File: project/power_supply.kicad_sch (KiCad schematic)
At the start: 20 parts, among them J1 USB_C_Receptacle_USB2.0_16P, U1 LD1117S33TR_SOT223, U2 LD1117S12TR_SOT223, U3 USBLC6-2SC6

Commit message: Ruteo critico finalizado
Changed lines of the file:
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@@
 (kicad_sch
-	(version 20231120)
+	(version 20250114)
 	(generator "eeschema")
-	(generator_version "8.0")
+	(generator_version "9.0")
 	(paper "A4")
 	(junction
@@
 		(shape bidirectional)
 		(at 93.98 93.98 0)
-		(fields_autoplaced yes)
 		(effects
 			(font
@@
 		(shape output)
 		(at 149.86 96.52 270)
-		(fields_autoplaced yes)
 		(effects
 			(font
@@
 		(shape output)
 		(at 143.51 72.39 90)
-		(fields_autoplaced yes)
 		(effects
 			(font
@@
 		(shape bidirectional)
 		(at 93.98 91.44 0)
-		(fields_autoplaced yes)
 		(effects
 			(font
@@
 		(shape output)
 		(at 189.23 73.66 90)
-		(fields_autoplaced yes)
 		(effects
 			(font
@@
 		(shape output)
 		(at 252.73 76.2 0)
-		(fields_autoplaced yes)
 		(effects
 			(font

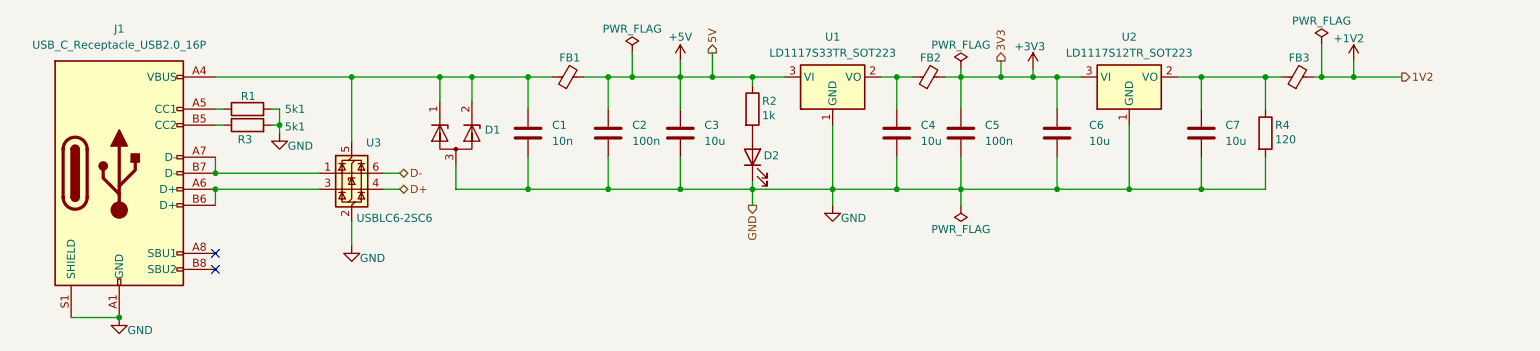
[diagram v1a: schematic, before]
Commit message: Agregado de datasheets, cambio de regulador zener, ajuste de posicion de regulador, modelo 3d de oscilador
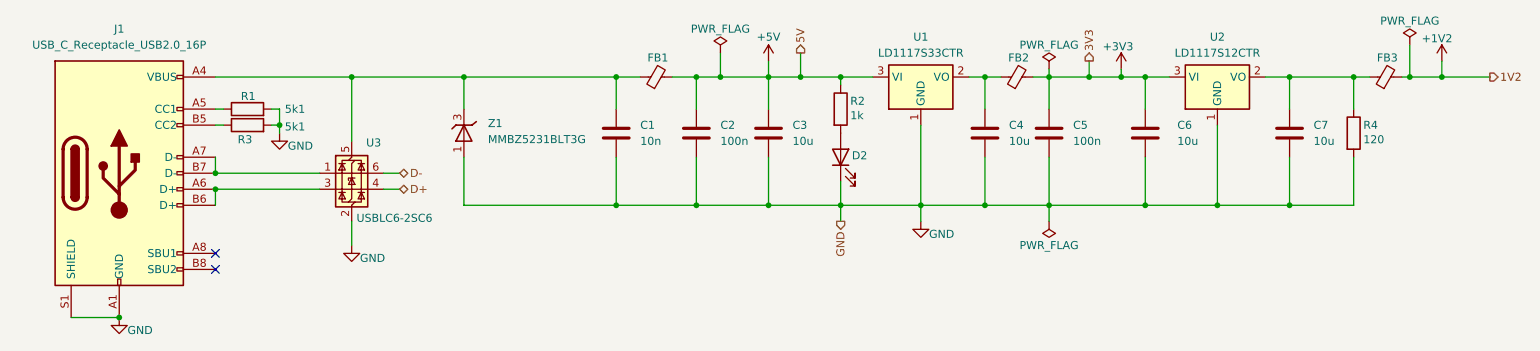
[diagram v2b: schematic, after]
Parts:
- removed D1: ~, Package_TO_SOT_SMD:SOT-23, symbol Diode:MMBZxx
- added Z1: MMBZ5231BLT3G, MMBZ5231BLT3G:SOT96P237X111-3N, symbol MMBZ5231BLT3G:MMBZ5231BLT3G
- C1: Código del fabricante (Order Code) (none) -> CL31B103KHFNFNE; Código del vendedor (Provider Order Code) (none) -> 187-CL31B103KHFNFNE; Fabricante (none) -> Samsung; Package (none) -> 1206
- C2, C5: Código del fabricante (Order Code) (none) -> CL31B104KBCNFNC; Código del vendedor (Provider Order Code) (none) -> 187-CL31B104KBCNFNC; Fabricante (none) -> Samsung; Package (none) -> 1206
- C3, C4, C6, C7: Código del fabricante (Order Code) (none) -> CL31B106KAHNNNE; Código del vendedor (Provider Order Code) (none) -> 187-CL31B106KAHNNNE; Fabricante (none) -> Samsung; Package (none) -> 1206
- D2: value LED Green -> LED Red; Código del fabricante (Order Code) (none) -> 150141RS73100; Código del vendedor (Provider Order Code) (none) -> 710-150141RS73100; Fabricante (none) -> Wurth Elektronik; Package (none) -> 3528
- FB1, FB2, FB3: Código del fabricante (Order Code) (none) -> 742792141; Código del vendedor (Provider Order Code) (none) -> 710-742792141; Fabricante (none) -> Wurth Elektronik; Package (none) -> 1206
- J1: Código del fabricante (Order Code) (none) -> GSB1C41110SSHR; Código del vendedor (Provider Order Code) (none) -> 523-GSB1C41110SSHR; Fabricante (none) -> Amphenol; Package (none) -> USB-C
- R1, R3: Código del fabricante (Order Code) (none) -> AC1206FR-075K1L; Código del vendedor (Provider Order Code) (none) -> 603-AC1206FR-075K1L; Fabricante (none) -> Yageo; Package (none) -> 1206
- R2: Código del fabricante (Order Code) (none) -> RC1206FR-101KL; Código del vendedor (Provider Order Code) (none) -> 603-RC1206FR-101KL; Fabricante (none) -> Yageo; Package (none) -> 1206
- R4: Código del fabricante (Order Code) (none) -> RC1206FR-07120RL; Código del vendedor (Provider Order Code) (none) -> 603-RC1206FR-07120RL; Fabricante (none) -> Yageo; Package (none) -> 1206
- U1: value LD1117S33TR_SOT223 -> LD1117S33CTR; Código del fabricante (Order Code) (none) -> LD1117S33CTR; Código del vendedor (Provider Order Code) (none) -> 511-LD1117S33CTR; Fabricante (none) -> ST; Package (none) -> SOT-223-3
- U2: value LD1117S12TR_SOT223 -> LD1117S12CTR; Código del fabricante (Order Code) (none) -> LD1117S12CTR; Código del vendedor (Provider Order Code) (none) -> 511-LD1117S12CTR; Fabricante (none) -> ST; Package (none) -> SOT-223-3
- U3: Código del fabricante (Order Code) (none) -> USBLC6-2SC6; Código del vendedor (Provider Order Code) (none) -> 511-USBLC6-2SC6; Fabricante (none) -> ST; Package (none) -> SOT-666-6
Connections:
- net GND: now also Z1.1
- net at C1.1, FB1.1, J1.A4 (VBUS)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: now also Z1.3
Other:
- moved on the sheet: C1, C2, C3, C4, C5, C6, C7, D2, FB1, FB2, FB3, R2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

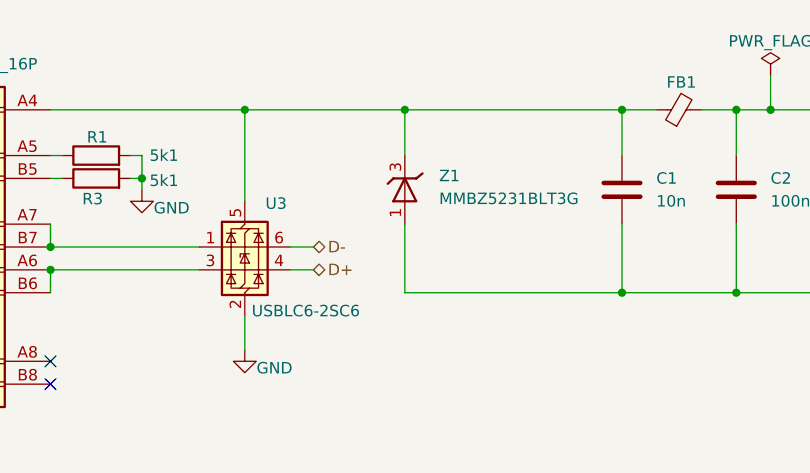
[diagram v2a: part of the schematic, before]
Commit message: Pistas, pads, soldermask y silkscreen corregidas para pasar analisis DMF de jlcpcb.
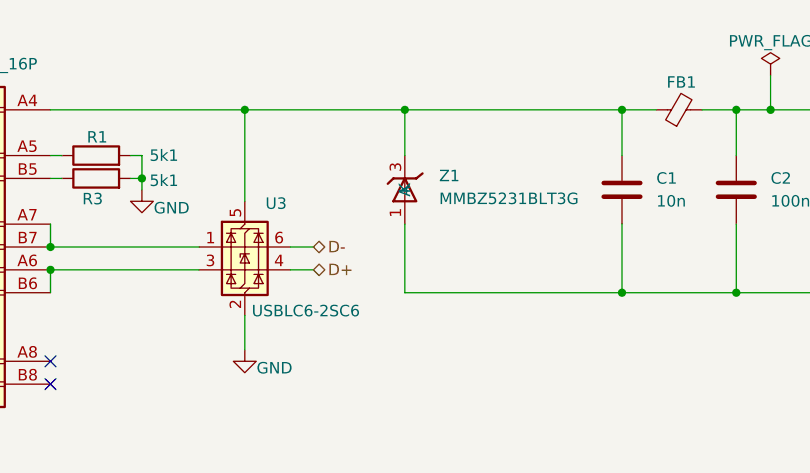
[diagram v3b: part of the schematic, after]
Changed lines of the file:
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@@
 			)
 		)
-		(property "Datasheet" "https://www.we-online.com/components/products/datasheet/150141RS73100.pdf"
+		(property "Datasheet" "~"
 			(at 163.83 88.9 0)
 			(effects
@@
 			(effects
 				(font
+					(size 1.27 1.27)
+				)
+				(hide yes)
+			)
+		)
+		(property "Sim.Pins" "1=K 2=A"
+			(at 163.83 88.9 0)
+			(effects
+				(font

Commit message: actualizacion readme
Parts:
- U3: Package SOT-666-6 -> SOT-23-6
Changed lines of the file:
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@@
 			)
 		)
-		(property "Package" "SOT-666-6"
+		(property "Package" "SOT-23-6"
 			(at 86.36 91.44 0)
 			(effects

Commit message: cambio a nombre final, agregado de licencia en esquematico y etiqueta
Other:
- company: (none) -> Maximiliano Simonazzi, Valentin Gomez Espeche
- title: (none) -> Azukar FPGA
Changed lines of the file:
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@@
 	(generator_version "9.0")
 	(paper "A4")
+	(title_block
+		(title "Azukar FPGA")
+		(date "2026-02-04")
+		(rev "1.4")
+		(company "Maximiliano Simonazzi, Valentin Gomez Espeche")
+		(comment 1 "attribution to the original AZUKAR project is preserved.")
+		(comment 2 "This design may be copied, modified, manufactured, and distributed provided that")
+		(comment 3 "Year: 2026")
+		(comment 4 "License: CERN Open Hardware Licence v2 – Permissive (CERN-OHL-P-2.0)")
+	)
 	(junction
 		(at 186.69 96.52)
@@
 		)
 		(instances
-			(project "fpga-utn"
+			(project "azukar-fpga"
 				(path "/fadb8841-cd7a-4174-937d-7c393e857c90/addbb95a-5ecf-43db-ab5f-45b593a9e920"
 					(reference "#PWR03")
@@
 		)
 		(instances
-			(project "fpga-utn"
+			(project "azukar-fpga"
 				(path "/fadb8841-cd7a-4174-937d-7c393e857c90/addbb95a-5ecf-43db-ab5f-45b593a9e920"
 					(reference "R4")
@@
 		)
 		(instances
-			(project "fpga-utn"
+			(project "azukar-fpga"
 				(path "/fadb8841-cd7a-4174-937d-7c393e857c90/addbb95a-5ecf-43db-ab5f-45b593a9e920"
 					(reference "#FLG03")
@@
 		)
 		(instances
-			(project "fpga-utn"
+			(project "azukar-fpga"
 				(path "/fadb8841-cd7a-4174-937d-7c393e857c90/addbb95a-5ecf-43db-ab5f-45b593a9e920"
 					(reference "C3")
@@
 		)
 		(instances
-			(project "fpga-utn"
+			(project "azukar-fpga"
 				(path "/fadb8841-cd7a-4174-937d-7c393e857c90/addbb95a-5ecf-43db-ab5f-45b593a9e920"
 					(reference "FB2")
@@
 		)
 		(instances
-			(project "fpga-utn"
+			(project "azukar-fpga"
 				(path "/fadb8841-cd7a-4174-937d-7c393e857c90/addbb95a-5ecf-43db-ab5f-45b593a9e920"
 					(reference "J1")
@@
 		)
 		(instances
-			(project "fpga-utn"
+			(project "azukar-fpga"
 				(path "/fadb8841-cd7a-4174-937d-7c393e857c90/addbb95a-5ecf-43db-ab5f-45b593a9e920"
 					(reference "C6")
@@
 		)
 		(instances
-			(project "fpga-utn"
+			(project "azukar-fpga"
 				(path "/fadb8841-cd7a-4174-937d-7c393e857c90/addbb95a-5ecf-43db-ab5f-45b593a9e920"
 					(reference "C2")
@@
 		)
 		(instances
-			(project "fpga-utn"
+			(project "azukar-fpga"
 				(path "/fadb8841-cd7a-4174-937d-7c393e857c90/addbb95a-5ecf-43db-ab5f-45b593a9e920"
 					(reference "#FLG02")
@@
 		)
 		(instances
-			(project "fpga-utn"
+			(project "azukar-fpga"
 				(path "/fadb8841-cd7a-4174-937d-7c393e857c90/addbb95a-5ecf-43db-ab5f-45b593a9e920"
 					(reference "#PWR07")
@@
 		)
 		(instances
-			(project "fpga-utn"
+			(project "azukar-fpga"
 				(path "/fadb8841-cd7a-4174-937d-7c393e857c90/addbb95a-5ecf-43db-ab5f-45b593a9e920"
 					(reference "C5")
@@
 		)
 		(instances
-			(project "fpga-utn"
+			(project "azukar-fpga"
 				(path "/fadb8841-cd7a-4174-937d-7c393e857c90/addbb95a-5ecf-43db-ab5f-45b593a9e920"
 					(reference "R1")
@@
 		)
 		(instances
-			(project "fpga-utn"
+			(project "azukar-fpga"
 				(path "/fadb8841-cd7a-4174-937d-7c393e857c90/addbb95a-5ecf-43db-ab5f-45b593a9e920"
 					(reference "FB1")
@@
 		)
 		(instances
-			(project "fpga-utn"
+			(project "azukar-fpga"
 				(path "/fadb8841-cd7a-4174-937d-7c393e857c90/addbb95a-5ecf-43db-ab5f-45b593a9e920"
 					(reference "C7")
@@
 		)
 		(instances
-			(project "fpga-utn"
+			(project "azukar-fpga"
 				(path "/fadb8841-cd7a-4174-937d-7c393e857c90/addbb95a-5ecf-43db-ab5f-45b593a9e920"
 					(reference "D2")
@@
 		)
 		(instances
-			(project "fpga-utn"
+			(project "azukar-fpga"
 				(path "/fadb8841-cd7a-4174-937d-7c393e857c90/addbb95a-5ecf-43db-ab5f-45b593a9e920"
 					(reference "C4")
@@
 		)
 		(instances
-			(project "fpga-utn"
+			(project "azukar-fpga"
 				(path "/fadb8841-cd7a-4174-937d-7c393e857c90/addbb95a-5ecf-43db-ab5f-45b593a9e920"
 					(reference "#PWR06")
@@
 		)
 		(instances
-			(project "fpga-utn"
+			(project "azukar-fpga"
 				(path "/fadb8841-cd7a-4174-937d-7c393e857c90/addbb95a-5ecf-43db-ab5f-45b593a9e920"
 					(reference "R2")
@@
 		)
 		(instances
-			(project "fpga-utn"
+			(project "azukar-fpga"
 				(path "/fadb8841-cd7a-4174-937d-7c393e857c90/addbb95a-5ecf-43db-ab5f-45b593a9e920"
 					(reference "#FLG04")
@@
 		)
 		(instances
-			(project "fpga-utn"
+			(project "azukar-fpga"
 				(path "/fadb8841-cd7a-4174-937d-7c393e857c90/addbb95a-5ecf-43db-ab5f-45b593a9e920"
 					(reference "R3")
@@
 		)
 		(instances
-			(project "fpga-utn"
+			(project "azukar-fpga"
 				(path "/fadb8841-cd7a-4174-937d-7c393e857c90/addbb95a-5ecf-43db-ab5f-45b593a9e920"
 					(reference "#PWR02")
@@
 		)
 		(instances
-			(project "fpga-utn"
+			(project "azukar-fpga"
 				(path "/fadb8841-cd7a-4174-937d-7c393e857c90/addbb95a-5ecf-43db-ab5f-45b593a9e920"
 					(reference "#FLG01")
@@
 		)
 		(instances
-			(project "fpga-utn"
+			(project "azukar-fpga"
 				(path "/fadb8841-cd7a-4174-937d-7c393e857c90/addbb95a-5ecf-43db-ab5f-45b593a9e920"
 					(reference "U3")
@@
 		)
 		(instances
-			(project "fpga-utn"
+			(project "azukar-fpga"
 				(path "/fadb8841-cd7a-4174-937d-7c393e857c90/addbb95a-5ecf-43db-ab5f-45b593a9e920"
 					(reference "#PWR05")
@@
 		)
 		(instances
-			(project "fpga-utn"
+			(project "azukar-fpga"
 				(path "/fadb8841-cd7a-4174-937d-7c393e857c90/addbb95a-5ecf-43db-ab5f-45b593a9e920"
 					(reference "FB3")
@@
 		)
 		(instances
-			(project "fpga-utn"
+			(project "azukar-fpga"
 				(path "/fadb8841-cd7a-4174-937d-7c393e857c90/addbb95a-5ecf-43db-ab5f-45b593a9e920"
 					(reference "#PWR01")
@@
 		)
 		(instances
-			(project "fpga-utn"
+			(project "azukar-fpga"
 				(path "/fadb8841-cd7a-4174-937d-7c393e857c90/addbb95a-5ecf-43db-ab5f-45b593a9e920"
 					(reference "#PWR04")

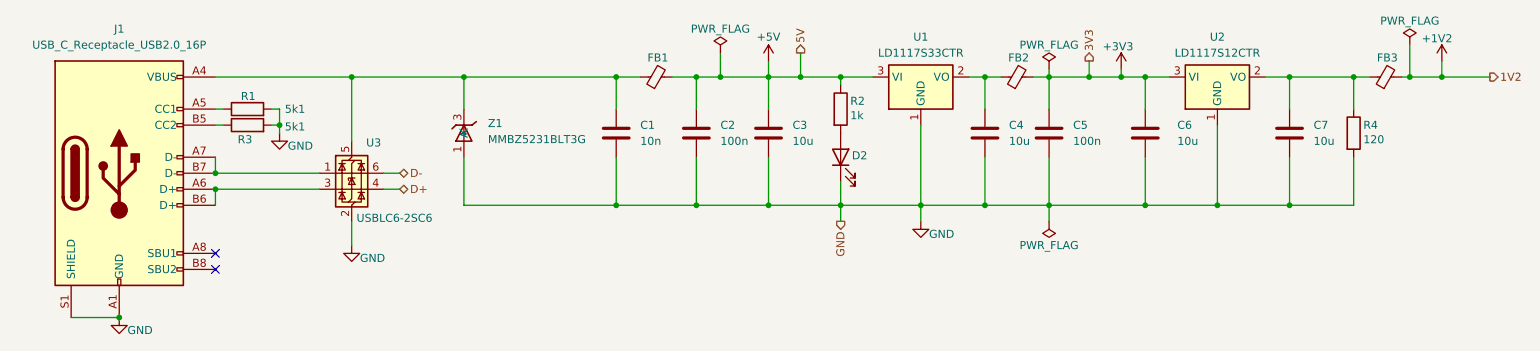
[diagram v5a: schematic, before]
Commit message: Eliminar mensaje de error - Issue #8. Mejora en algunas trazas del PCB, eliminacion de algunas vias ordenando mejor los componentes.
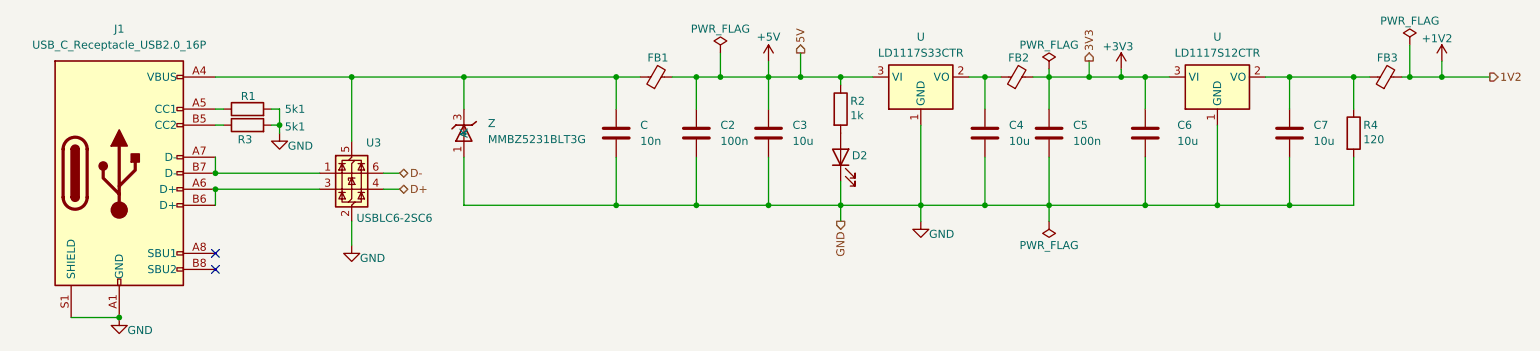
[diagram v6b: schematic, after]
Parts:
- renumbered C1 to C, U1 to U, U2 to U, Z1 to Z
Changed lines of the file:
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@@
 		(dnp no)
 		(fields_autoplaced yes)
-		(property "Reference" "U1"
+		(property "Reference" "U"
 			(at 176.53 69.85 0)
 			(effects
@@
 		(pin "1"
 		)
-		(instances
-			(project ""
-				(path "/fadb8841-cd7a-4174-937d-7c393e857c90/addbb95a-5ecf-43db-ab5f-45b593a9e920"
-					(reference "U1")
-					(unit 1)
-				)
-			)
-		)
+		(instances)
 	)
 	(symbol
@@
 		(dnp no)
 		(fields_autoplaced yes)
-		(property "Reference" "U2"
+		(property "Reference" "U"
 			(at 223.52 69.85 0)
 			(effects
@@
 		(pin "3"
 		)
-		(instances
-			(project ""
-				(path "/fadb8841-cd7a-4174-937d-7c393e857c90/addbb95a-5ecf-43db-ab5f-45b593a9e920"
-					(reference "U2")
-					(unit 1)
-				)
-			)
-		)
+		(instances)
 	)
 	(symbol
@@
 		(dnp no)
 		(fields_autoplaced yes)
-		(property "Reference" "C1"
+		(property "Reference" "C"
 			(at 132.08 83.8199 0)
 			(effects
@@
 		(pin "2"
 		)
-		(instances
-			(project ""
-				(path "/fadb8841-cd7a-4174-937d-7c393e857c90/addbb95a-5ecf-43db-ab5f-45b593a9e920"
-					(reference "C1")
-					(unit 1)
-				)
-			)
-		)
+		(instances)
 	)
 	(symbol
@@
 		(dnp no)
 		(fields_autoplaced yes)
-		(property "Reference" "Z1"
+		(property "Reference" "Z"
 			(at 107.95 83.5421 90)
 			(effects
@@
 		(pin "3"
 		)
-		(instances
-			(project ""
-				(path "/fadb8841-cd7a-4174-937d-7c393e857c90/addbb95a-5ecf-43db-ab5f-45b593a9e920"
-					(reference "Z1")
-					(unit 1)
-				)
-			)
-		)
+		(instances)
 	)
 	(symbol

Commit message: Eliminar mensaje de error - Issue #8. Mejora en algunas trazas del PCB, eliminacion de algunas vias ordenando mejor los componentes.
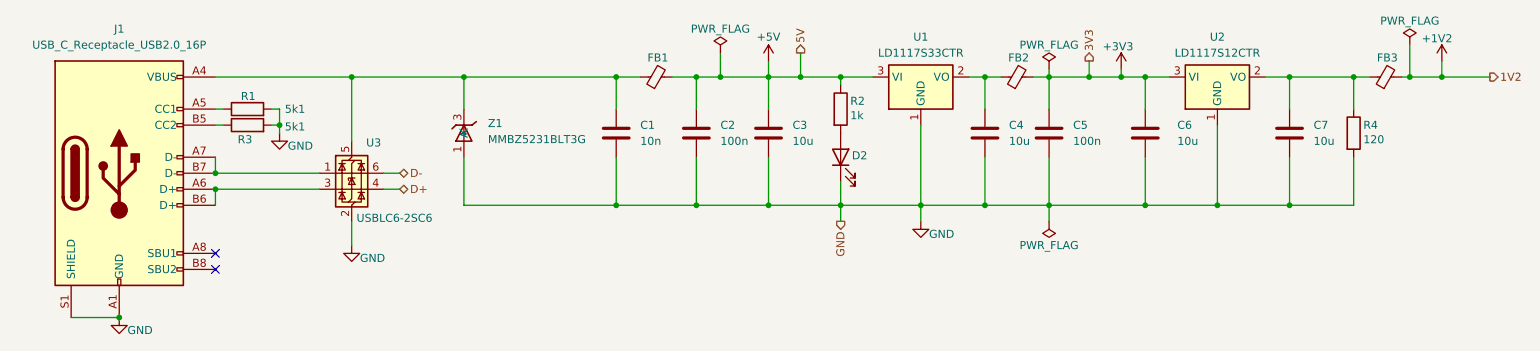
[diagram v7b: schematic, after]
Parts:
- renumbered C to C1, U to U1, U to U2, Z to Z1
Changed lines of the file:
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@@
 		(dnp no)
 		(fields_autoplaced yes)
-		(property "Reference" "U"
+		(property "Reference" "U1"
 			(at 176.53 69.85 0)
 			(effects
@@
 		(pin "1"
 		)
-		(instances)
+		(instances
+			(project "azukar-fpga"
+				(path "/fadb8841-cd7a-4174-937d-7c393e857c90/addbb95a-5ecf-43db-ab5f-45b593a9e920"
+					(reference "U1")
+					(unit 1)
+				)
+			)
+		)
 	)
 	(symbol
@@
 		(dnp no)
 		(fields_autoplaced yes)
-		(property "Reference" "U"
+		(property "Reference" "U2"
 			(at 223.52 69.85 0)
 			(effects
@@
 		(pin "3"
 		)
-		(instances)
+		(instances
+			(project "azukar-fpga"
+				(path "/fadb8841-cd7a-4174-937d-7c393e857c90/addbb95a-5ecf-43db-ab5f-45b593a9e920"
+					(reference "U2")
+					(unit 1)
+				)
+			)
+		)
 	)
 	(symbol
@@
 		(dnp no)
 		(fields_autoplaced yes)
-		(property "Reference" "C"
+		(property "Reference" "C1"
 			(at 132.08 83.8199 0)
 			(effects
@@
 		(pin "2"
 		)
-		(instances)
+		(instances
+			(project "azukar-fpga"
+				(path "/fadb8841-cd7a-4174-937d-7c393e857c90/addbb95a-5ecf-43db-ab5f-45b593a9e920"
+					(reference "C1")
+					(unit 1)
+				)
+			)
+		)
 	)
 	(symbol
@@
 		(dnp no)
 		(fields_autoplaced yes)
-		(property "Reference" "Z"
+		(property "Reference" "Z1"
 			(at 107.95 83.5421 90)
 			(effects
@@
 		(pin "3"
 		)
-		(instances)
+		(instances
+			(project "azukar-fpga"
+				(path "/fadb8841-cd7a-4174-937d-7c393e857c90/addbb95a-5ecf-43db-ab5f-45b593a9e920"
+					(reference "Z1")
+					(unit 1)
+				)
+			)
+		)
 	)
 	(symbol

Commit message: Version 2 de pcb completa, falta revisar silkscreen y ajustes menores
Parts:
- renumbered D2 to D1
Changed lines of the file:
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@@
 		(title "Azukar FPGA")
 		(date "2026-02-04")
-		(rev "1.4")
+		(rev "2.0")
 		(company "Maximiliano Simonazzi, Valentin Gomez Espeche")
 		(comment 1 "attribution to the original AZUKAR project is preserved.")
@@
 		(on_board yes)
 		(dnp no)
-		(property "Reference" "D2"
+		(property "Reference" "D1"
 			(at 165.608 88.646 90)
 			(effects
@@
 			(project "azukar-fpga"
 				(path "/fadb8841-cd7a-4174-937d-7c393e857c90/addbb95a-5ecf-43db-ab5f-45b593a9e920"
-					(reference "D2")
+					(reference "D1")
 					(unit 1)
 				)
